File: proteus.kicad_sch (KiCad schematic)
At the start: 29 parts, among them J1 Conn_01x01, J15 Sicma_56, J2 Conn_01x01, J3 Conn_01x01, J4 Conn_01x03, J5 Conn_01x05, J6 Conn_02x04_Counter_Clockwise, J9 Conn_01x04

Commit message: Several optimizations
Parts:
- added J13: Conn_01x03, Connector_PinHeader_2.54mm:PinHeader_1x03_P2.54mm_Vertical, symbol Connector_Generic:Conn_01x03
- J5: footprint Connector_PinHeader_2.54mm:PinHeader_1x05_P2.54mm_Vertical -> Connector_PinHeader_2.54mm:PinHeader_1x06_P2.54mm_Vertical; symbol Connector_Generic:Conn_01x05 -> Connector_Generic:Conn_01x06
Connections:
- net 5V_SENSOR_1: now also J5.1 (Pin_1)
- net GND: now also J5.6 (Pin_6), J13.3 (Pin_3); no longer J5.5 (Pin_5)
- net quad_analog3/IN2: now also J5.4 (Pin_4); no longer J5.3 (Pin_3)
- net quad_analog3/IN3: now also J5.5 (Pin_5); no longer J5.4 (Pin_4)
- net quad_analog_temp/IN3: now also J5.3 (Pin_3); no longer J5.2 (Pin_2)
- net quad_analog_temp/IN4: now also J5.2 (Pin_2); no longer J5.1 (Pin_1)
- new net triggers/HALL_IN_5: J13.1 (Pin_1)
- new net triggers/HALL_IN_6: J13.2 (Pin_2)
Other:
- sheet triggers ports: added HALL_IN_5, HALL_IN_6, HALL_OUT_5, HALL_OUT_6; removed none
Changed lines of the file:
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@@
   (junction (at 272.415 84.455) (diameter 0) (color 0 0 0 0)
   )
+  (junction (at 29.845 88.265) (diameter 0) (color 0 0 0 0)
+  )
   (junction (at 203.2 132.715) (diameter 0) (color 0 0 0 0)
   )
@@
     (stroke (width 0) (type default))
   )
-  (wire (pts (xy 31.115 73.66) (xy 23.495 73.66))
+  (wire (pts (xy 31.115 73.66) (xy 20.955 73.66))
     (stroke (width 0) (type default))
   )
@@
     (stroke (width 0) (type default))
   )
+  (wire (pts (xy 29.21 149.86) (xy 34.29 149.86))
+    (stroke (width 0) (type default))
+  )
   (wire (pts (xy 114.3 67.31) (xy 120.65 67.31))
     (stroke (width 0) (type default))
@@
     (stroke (width 0) (type default))
   )
+  (wire (pts (xy 29.845 76.2) (xy 20.955 76.2))
+    (stroke (width 0) (type default))
+  )
   (wire (pts (xy 200.66 113.03) (xy 209.55 113.03))
     (stroke (width 0) (type default))
@@
     (stroke (width 0) (type default))
   )
+  (wire (pts (xy 29.21 150.495) (xy 29.21 149.86))
+    (stroke (width 0) (type default))
+  )
   (wire (pts (xy 53.975 124.46) (xy 68.58 124.46))
     (stroke (width 0) (type default))
   )
+  (wire (pts (xy 26.67 88.265) (xy 29.845 88.265))
+    (stroke (width 0) (type default))
+  )
   (wire (pts (xy 257.81 84.455) (xy 272.415 84.455))
     (stroke (width 0) (type default))
@@
     (stroke (width 0) (type default))
   )
+  (wire (pts (xy 27.94 147.955) (xy 34.29 147.955))
+    (stroke (width 0) (type default))
+  )
   (wire (pts (xy 68.58 130.81) (xy 53.975 130.81))
     (stroke (width 0) (type default))
@@
     (stroke (width 0) (type default))
   )
-  (wire (pts (xy 23.495 68.58) (xy 33.655 68.58))
+  (wire (pts (xy 20.955 68.58) (xy 33.655 68.58))
     (stroke (width 0) (type default))
   )
@@
     (stroke (width 0) (type default))
   )
+  (wire (pts (xy 62.23 147.955) (xy 68.58 147.955))
+    (stroke (width 0) (type default))
+  )
   (wire (pts (xy 114.3 95.885) (xy 122.555 95.885))
     (stroke (width 0) (type default))
@@
     (stroke (width 0) (type default))
   )
+  (wire (pts (xy 62.23 149.86) (xy 68.58 149.86))
+    (stroke (width 0) (type default))
+  )
   (wire (pts (xy 62.23 179.07) (xy 62.23 189.865))
     (stroke (width 0) (type default))
@@
     (stroke (width 0) (type default))
   )
-  (wire (pts (xy 23.495 71.12) (xy 33.655 71.12))
+  (wire (pts (xy 20.955 71.12) (xy 33.655 71.12))
     (stroke (width 0) (type default))
   )
@@
     (stroke (width 0) (type default))
   )
-  (wire (pts (xy 23.495 66.04) (xy 35.56 66.04))
+  (wire (pts (xy 20.955 66.04) (xy 35.56 66.04))
     (stroke (width 0) (type default))
   )
@@
     (stroke (width 0) (type default))
   )
+  (wire (pts (xy 29.21 150.495) (xy 27.94 150.495))
+    (stroke (width 0) (type default))
+  )
   (wire (pts (xy 120.65 41.275) (xy 114.3 41.275))
     (stroke (width 0) (type default))
@@
     (stroke (width 0) (type default))
   )
+  (wire (pts (xy 29.845 76.2) (xy 29.845 88.265))
+    (stroke (width 0) (type default))
+  )
   (wire (pts (xy 123.825 158.75) (xy 114.3 158.75))
     (stroke (width 0) (type default))
@@
     (stroke (width 0) (type default))
   )
-  (wire (pts (xy 22.86 88.265) (xy 37.465 88.265))
+  (wire (pts (xy 29.845 88.265) (xy 37.465 88.265))
     (stroke (width 0) (type default))
   )
@@
     (effects (font (size 1.27 1.27)) (justify left bottom))
   )
-  (label "5V_SENSOR_1" (at 22.86 88.265 0) (fields_autoplaced)
-    (effects (font (size 1.27 1.27)) (justify left bottom))
+  (label "5V_SENSOR_1" (at 26.67 88.265 180) (fields_autoplaced)
+    (effects (font (size 1.27 1.27)) (justify right bottom))
   )
   (label "LS8" (at 232.41 61.595 180) (fields_autoplaced)
@@
     )
   )
+  (symbol (lib_id "power:GND") (at 27.94 153.035 90) (unit 1)
+    (in_bom yes) (on_board yes) (dnp no)
+    (property "Reference" "#PWR0265" (at 34.29 153.035 0)
+      (effects (font (size 1.27 1.27)) hide)
+    )
+    (property "Value" "GND" (at 32.3342 152.908 0)
+      (effects (font (size 1.27 1.27)))
+    )
+    (property "Footprint" "" (at 27.94 153.035 0)
+      (effects (font (size 1.27 1.27)) hide)
+    )
+    (property "Datasheet" "" (at 27.94 153.035 0)
+      (effects (font (size 1.27 1.27)) hide)
+    )
+    (pin "1")
+    (instances
+      (project "proteus"
+        (path "/d9116601-cae2-4199-827b-70fa136aae51"
+          (reference "#PWR0265") (unit 1)
+        )
+      )
+    )
+  )
   (symbol (lib_id "power:GND") (at 203.2 132.715 0) (unit 1)
     (in_bom yes) (on_board yes) (dnp no)
@@
     )
   )
-  (symbol (lib_id "power:GND") (at 23.495 63.5 90) (unit 1)
-    (in_bom yes) (on_board yes) (dnp no)
-    (property "Reference" "#PWR011" (at 29.845 63.5 0)
-      (effects (font (size 1.27 1.27)) hide)
-    )
-    (property "Value" "GND" (at 27.8892 63.373 0)
+  (symbol (lib_id "power:GND") (at 20.955 63.5 90) (unit 1)
+    (in_bom yes) (on_board yes) (dnp no)
+    (property "Reference" "#PWR011" (at 27.305 63.5 0)
+      (effects (font (size 1.27 1.27)) hide)
+    )
+    (property "Value" "GND" (at 25.3492 63.373 0)
       (effects (font (size 1.27 1.27)))
     )
-    (property "Footprint" "" (at 23.495 63.5 0)
-      (effects (font (size 1.27 1.27)) hide)
-    )
-    (property "Datasheet" "" (at 23.495 63.5 0)
+    (property "Footprint" "" (at 20.955 63.5 0)
+      (effects (font (size 1.27 1.27)) hide)
+    )
+    (property "Datasheet" "" (at 20.955 63.5 0)
       (effects (font (size 1.27 1.27)) hide)
     )
@@
     )
   )
+  (symbol (lib_id "Connector_Generic:Conn_01x03") (at 22.86 150.495 0) (mirror y) (unit 1)
+    (in_bom yes) (on_board yes) (dnp no)
+    (property "Reference" "J13" (at 20.32 150.495 90)
+      (effects (font (size 1.27 1.27)) (justify left))
+    )
+    (property "Value" "Conn_01x03" (at 20.955 144.78 90)
+      (effects (font (size 1.27 1.27)) (justify left) hide)
+    )
+    (property "Footprint" "Connector_PinHeader_2.54mm:PinHeader_1x03_P2.54mm_Vertical" (at 22.86 150.495 0)
+      (effects (font (size 1.27 1.27)) hide)
+    )
+    (property "Datasheet" "~" (at 22.86 150.495 0)
+      (effects (font (size 1.27 1.27)) hide)
+    )
+    (pin "1")
+    (pin "2")
+    (pin "3")
+    (instances
+      (project "proteus"
+        (path "/d9116601-cae2-4199-827b-70fa136aae51"
+          (reference "J13") (unit 1)
+        )
+      )
+    )
+  )
   (symbol (lib_id "Device:Polyfuse") (at 197.485 152.4 90) (unit 1)
     (in_bom yes) (on_board yes) (dnp no)
@@
     )
   )
-  (symbol (lib_id "Connector_Generic:Conn_01x05") (at 18.415 68.58 180) (unit 1)
-    (in_bom yes) (on_board yes) (dnp no)
-    (property "Reference" "J5" (at 18.415 60.96 0)
+  (symbol (lib_id "Connector_Generic:Conn_01x06") (at 15.875 71.12 180) (unit 1)
+    (in_bom yes) (on_board yes) (dnp no)
+    (property "Reference" "J5" (at 15.875 63.5 0)
       (effects (font (size 1.27 1.27)))
     )
-    (property "Value" "Conn_01x05" (at 18.415 60.96 0)
-      (effects (font (size 1.27 1.27)) hide)
-    )
-    (property "Footprint" "Connector_PinHeader_2.54mm:PinHeader_1x05_P2.54mm_Vertical" (at 18.415 68.58 0)
-      (effects (font (size 1.27 1.27)) hide)
-    )
-    (property "Datasheet" "~" (at 18.415 68.58 0)
+    (property "Value" "Conn_01x05" (at 15.875 63.5 0)
+      (effects (font (size 1.27 1.27)) hide)
+    )
+    (property "Footprint" "Connector_PinHeader_2.54mm:PinHeader_1x06_P2.54mm_Vertical" (at 15.875 71.12 0)
+      (effects (font (size 1.27 1.27)) hide)
+    )
+    (property "Datasheet" "~" (at 15.875 71.12 0)
       (effects (font (size 1.27 1.27)) hide)
     )
@@
     (pin "4")
     (pin "5")
+    (pin "6")
     (instances
       (project "proteus"
@@
       (effects (font (size 1.27 1.27)) (justify right))
     )
-    (instances
+    (pin "HALL_OUT_6" output (at 62.23 149.86 0)
+      (effects (font (size 1.27 1.27)) (justify right))
+    )
+    (pin "HALL_OUT_5" output (at 62.23 147.955 0)
+      (effects (font (size 1.27 1.27)) (justify right))
+    )
+    (pin "HALL_IN_5" input (at 34.29 147.955 180)
+      (effects (font (size 1.27 1.27)) (justify left))
+    )
+    (pin "HALL_IN_6" input (at 34.29 149.86 180)
+      (effects (font (size 1.27 1.27)) (justify left))
+    )
+    (instances

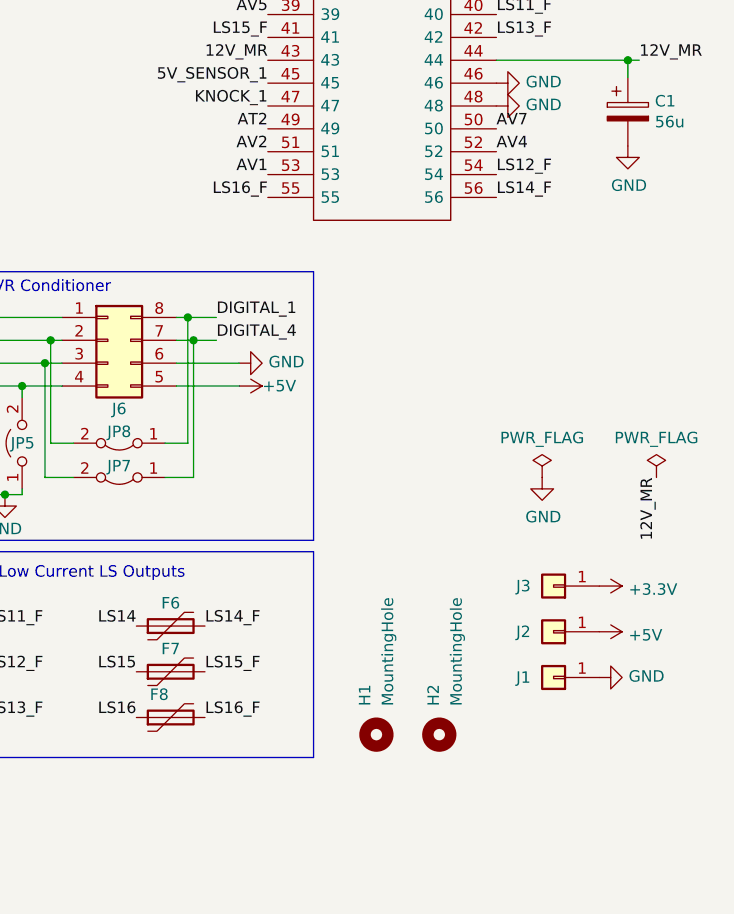
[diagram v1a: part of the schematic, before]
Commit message: Fix connector, optimize psu
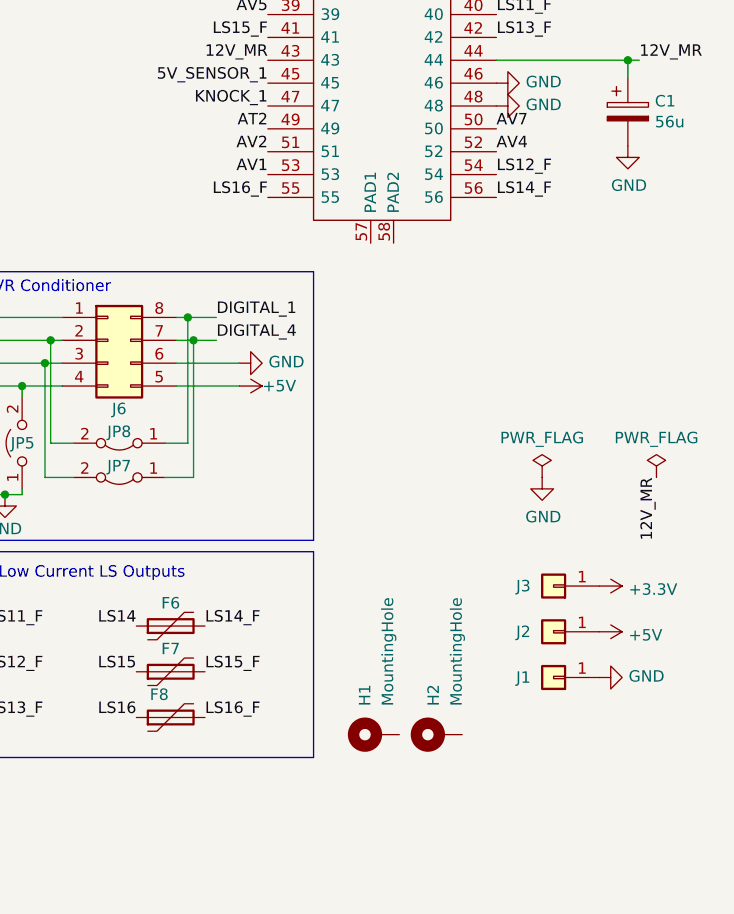
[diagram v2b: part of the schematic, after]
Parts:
- D1, D2, D3, D4: LCSC C8678 -> C15874
- H1, H2: symbol Mechanical:MountingHole -> Mechanical:MountingHole_Pad
- J6: footprint Package_DIP:DIP-8_W7.62mm -> connector:DIP-8_W7.62mm_Socket_VR
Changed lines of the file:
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@@
       (effects (font (size 1.27 1.27)) hide)
     )
-    (property "LCSC" "C8678" (at 158.115 74.93 0)
+    (property "LCSC" "C15874" (at 158.115 74.93 0)
       (effects (font (size 1.27 1.27)) hide)
     )
@@
       (effects (font (size 1.27 1.27)) hide)
     )
-    (property "LCSC" "C8678" (at 158.115 71.12 0)
+    (property "LCSC" "C15874" (at 158.115 71.12 0)
       (effects (font (size 1.27 1.27)) hide)
     )
@@
       (effects (font (size 1.27 1.27)) hide)
     )
-    (property "LCSC" "C8678" (at 158.115 67.31 0)
+    (property "LCSC" "C15874" (at 158.115 67.31 0)
       (effects (font (size 1.27 1.27)) hide)
     )
@@
       (effects (font (size 1.27 1.27)) hide)
     )
-    (property "Footprint" "Package_DIP:DIP-8_W7.62mm" (at 214.63 115.57 0)
+    (property "Footprint" "connector:DIP-8_W7.62mm_Socket_VR" (at 214.63 115.57 0)
       (effects (font (size 1.27 1.27)) hide)
     )
@@
     )
   )
-  (symbol (lib_id "Mechanical:MountingHole") (at 251.46 159.385 90) (unit 1)
+  (symbol (lib_id "Mechanical:MountingHole_Pad") (at 251.46 159.385 90) (unit 1)
     (in_bom yes) (on_board yes) (dnp no) (fields_autoplaced)
     (property "Reference" "H2" (at 250.825 156.21 0)
@@
       (effects (font (size 1.27 1.27)) hide)
     )
+    (pin "1")
     (instances
       (project "proteus"
@@
       (effects (font (size 1.27 1.27)) hide)
     )
-    (property "LCSC" "C8678" (at 158.115 63.5 0)
+    (property "LCSC" "C15874" (at 158.115 63.5 0)
       (effects (font (size 1.27 1.27)) hide)
     )
@@
     )
   )
-  (symbol (lib_id "Mechanical:MountingHole") (at 244.475 159.385 90) (unit 1)
+  (symbol (lib_id "Mechanical:MountingHole_Pad") (at 244.475 159.385 90) (unit 1)
     (in_bom yes) (on_board yes) (dnp no) (fields_autoplaced)
     (property "Reference" "H1" (at 243.2049 156.21 0)
@@
       (effects (font (size 1.27 1.27)) hide)
     )
+    (pin "1")
     (instances
       (project "proteus"
@@
     (pin "8")
     (pin "9")
-    (instances
-      (project "proteus"
+    (pin "57")
+    (pin "58")
+    (instances
+      (project "proteus"
